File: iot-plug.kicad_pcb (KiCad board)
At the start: 2 copper layers, 55.4 x 52.2 mm, 32 parts, among them J1 Conn_01x02_Pin, J2 Conn_01x02_Pin, J3 USB_C_Receptacle_USB2.0_16P, K1 HF46F_005-HS1, Q2 2N3904, U1 ESP32-S3-MINI-1, U2 USBLC6-2SC6, U4 AMS1117-3.3

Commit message: from shivpc
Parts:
- added REF**: Symbol_HighVoltage_NoTriangle_2x5mm_Copper, Symbol:Symbol_HighVoltage_NoTriangle_2x5mm_Copper, F.Cu at (88.0, 100.5)

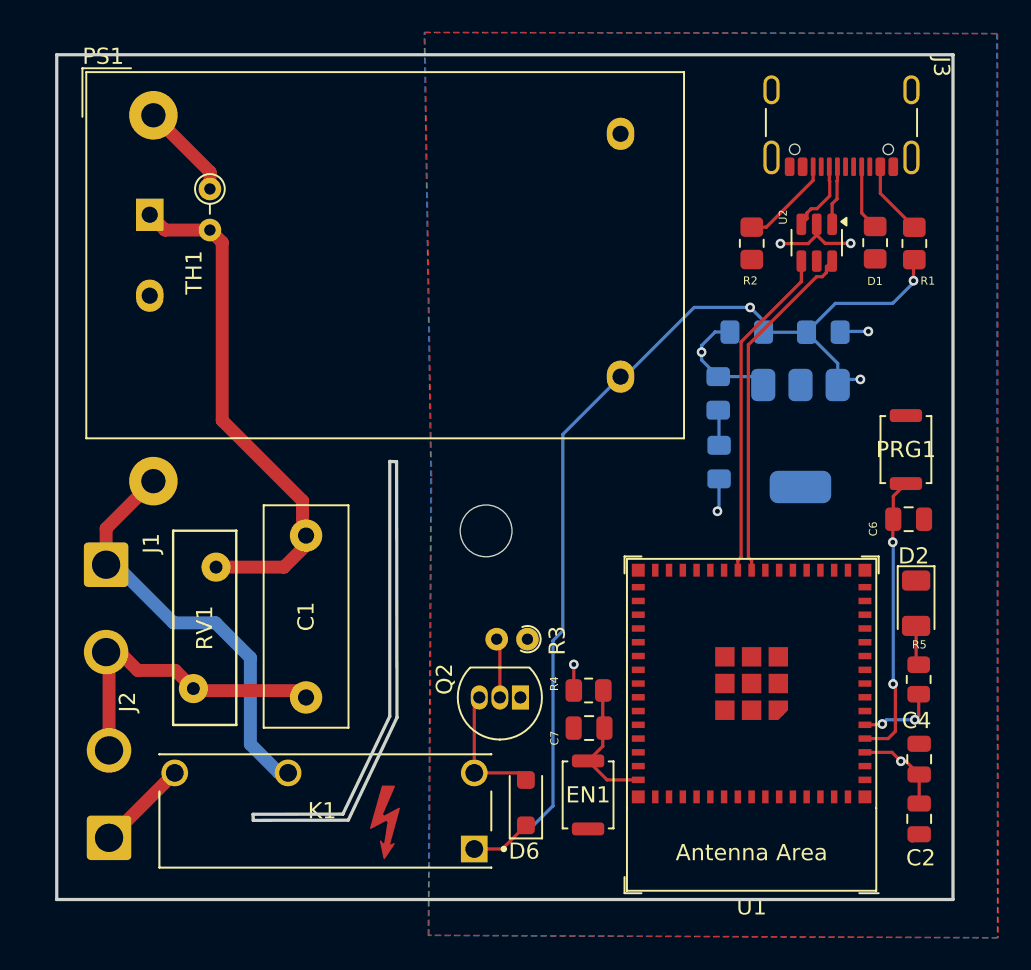
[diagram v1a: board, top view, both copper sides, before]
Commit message: layout updated
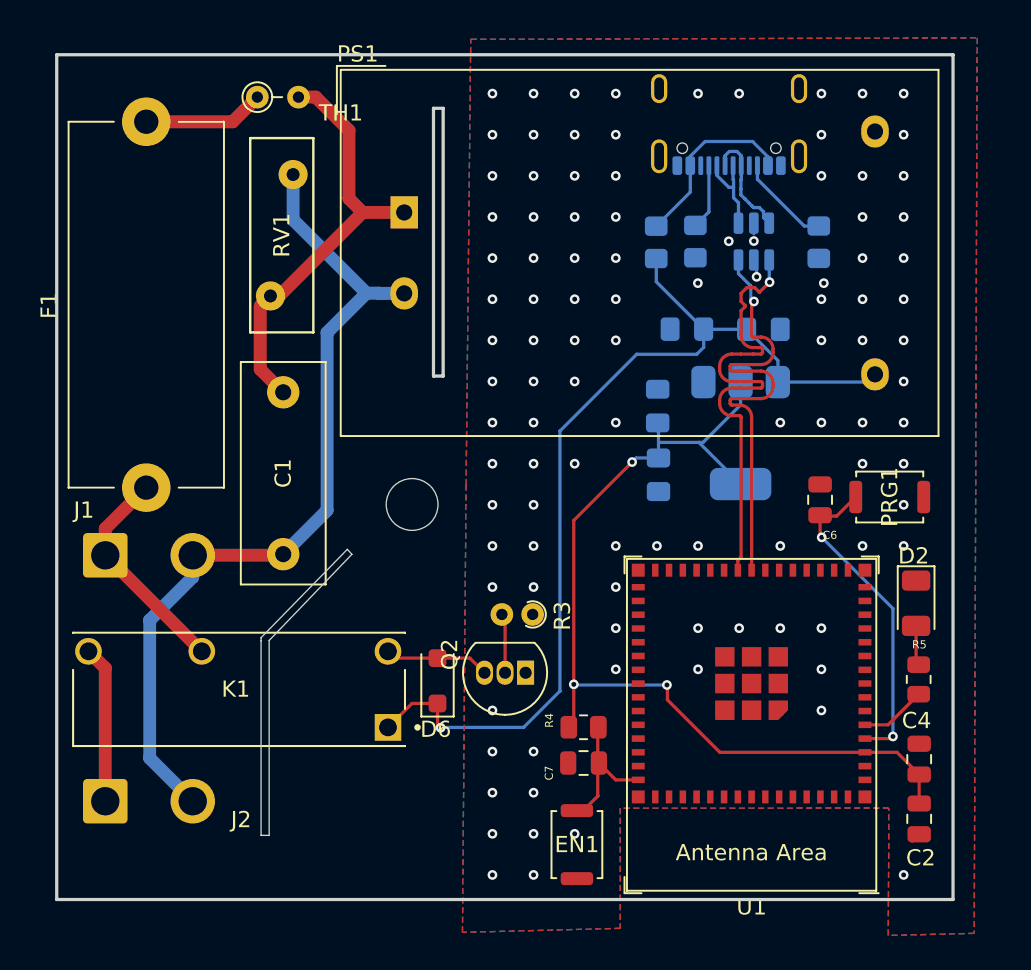
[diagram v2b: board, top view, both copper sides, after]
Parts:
- removed REF**: Symbol_HighVoltage_NoTriangle_2x5mm_Copper, Symbol:Symbol_HighVoltage_NoTriangle_2x5mm_Copper
- D1, J3, R1, R2, U2: moved to B.Cu
- F1: moved to F.Cu
- moved RV1 17.1 mm to (80.7, 67.8), turned to 90 degrees
- moved D1 15.9 mm to (104.5, 64.5)
- moved PS1 15.7 mm to (88.9, 62.7)
- moved R1 11.1 mm to (106.9, 64.5)
- moved D6 9.30 mm to (91.0, 91.6)
- moved K1 9.21 mm to (78.7, 92.1)
- moved C1 8.96 mm to (81.5, 73.8)
- moved J3 6.94 mm to (109.0, 56.1), turned to 0 degrees
- moved TH1 6.38 mm to (79.9, 55.6), turned to 0 degrees
- moved C6 5.60 mm to (114.6, 80.4), turned to 90 degrees
- moved H1 4.85 mm to (89.4, 80.7)
- moved R2 4.14 mm to (114.5, 64.5)
- moved U2 3.89 mm to (110.5, 64.5)
- moved C5 3.82 mm to (104.6, 74.6)
- moved CP2 3.82 mm to (104.7, 78.9)
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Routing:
- net 3V3: track 9.53 -> 58.9 mm, vias 2 -> 3
- net /N: track 19.7 -> 52.8 mm
- net GND: track 19.0 -> 3.33 mm, vias 5 -> 103
- net /P: track 26.1 -> 13.6 mm
- net /D+: track 25.2 -> 36.6 mm, vias 0 -> 1
- net /D-: track 25.2 -> 33.9 mm, vias 0 -> 1
- net Net-(D1-A): track 4.61 -> 11.3 mm
- net Net-(PS1-AC/L): track 32.7 -> 26.6 mm
- net L: track 5.72 -> 9.69 mm
- net 5V: track 63.5 -> 60.3 mm, vias 3 -> 1
- net /IO0: track 17.8 -> 20.5 mm
- net Net-(D6-A): track 8.16 -> 6.51 mm
- net Net-(F1-Pad2): track 6.00 -> 7.49 mm
- net /IO1: track 4.89 -> 4.10 mm, vias 2 -> 0
- added copper zone on B.Cu, net GND
- removed copper zone on B.Cu, net 3V3
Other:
- outline, holes or cut-outs redrawn

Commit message: logo added
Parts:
- added G***: LOGO, LOGO, F.Cu at (97.4, 81.4)
- added REF**: KiCad-Logo2_8mm_SilkScreen, Symbol:KiCad-Logo2_8mm_SilkScreen, F.Cu at (150.4, 87.0)
- added REF**: KiCad-Logo2_8mm_SilkScreen, Symbol:KiCad-Logo2_8mm_SilkScreen, F.Cu at (141.4, 86.5)
- moved H1 1.62 mm to (89.4, 82.3)
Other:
- board text added: "230V,10A"
- board text added: "AR RoboTics"
- board text added: "Home PlugX"
- board text added: "LOAD"
- board text added: "Made in India"

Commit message: updated tracks & nets
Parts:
- removed REF** (x2): KiCad-Logo2_8mm_SilkScreen, Symbol:KiCad-Logo2_8mm_SilkScreen
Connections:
- U1 pad 25: unconnected-(U1-GPIO21-Pad25) -> RL
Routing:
- net RL: track 0.00 -> 13.7 mm, vias 0 -> 1
- net 5V: track 60.3 -> 59.3 mm, vias 1 -> 5

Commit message: updated
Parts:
- moved J2 0.79 mm to (70.4, 99.8)
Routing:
- net /N: track 52.8 -> 53.5 mm
- net L: track 9.69 -> 10.4 mm
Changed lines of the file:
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@@
 	(footprint "Connector_Wire:SolderWire-1sqmm_1x02_P5.4mm_D1.4mm_OD2.7mm"
 		(layer "F.Cu")
-		(at 70.48 99.05)
+		(at 70.36 99.83)
 		(descr "Soldered wire connection, for 2 times 1 mm² wires, basic insulation, conductor diameter 1.4mm, outer diameter 2.7mm, size source Multi-Contact FLEXI-E 1.0 (https://ec.staubli.com/AcroFiles/Catalogues/TM_Cab-Main-11014119_(en)_hi.pdf), bend radius 3 times outer diameter, generated with kicad-footprint-generator")
 		(tags "connector wire 1sqmm")
@@
 	)
 	(gr_text "LOAD"
-		(at 71.12 103.45 0)
+		(at 71.03 103.95 0)
 		(layer "F.SilkS")
 		(effects
@@
 	)
 	(segment
-		(start 75.88 99.05)
-		(end 73.22 96.39)
+		(start 84.1765 81.0835)
+		(end 81.47 83.79)
 		(width 0.8)
 		(layer "B.Cu")
@@
 	)
 	(segment
-		(start 84.1765 81.0835)
-		(end 81.47 83.79)
+		(start 75.76 99.83)
+		(end 75.76 98.93)
 		(width 0.8)
 		(layer "B.Cu")
@@
 	)
 	(segment
-		(start 75.88 84.95)
-		(end 75.88 83.86)
+		(start 75.76 98.93)
+		(end 73.22 96.39)
 		(width 0.8)
 		(layer "B.Cu")
@@
 	)
 	(segment
-		(start 86.61 67.67)
-		(end 87.385 67.67)
+		(start 73.22 96.39)
+		(end 73.22 87.61)
 		(width 0.8)
 		(layer "B.Cu")
@@
 	)
 	(segment
-		(start 82.08 60.34)
-		(end 82.08 63.14)
+		(start 86.61 67.67)
+		(end 87.385 67.67)
 		(width 0.8)
 		(layer "B.Cu")
@@
 	)
 	(segment
-		(start 73.22 96.39)
-		(end 73.22 87.61)
+		(start 82.08 60.34)
+		(end 82.08 63.14)
+		(width 0.8)
+		(layer "B.Cu")
+		(net 51)
+	)
+	(segment
+		(start 75.88 84.95)
+		(end 75.88 83.86)
 		(width 0.8)
 		(layer "B.Cu")
@@
 	)
 	(segment
-		(start 69.87 98.44)
-		(end 69.87 90.22)
+		(start 70.36 99.83)
+		(end 70.36 98.93)
 		(width 0.8)
 		(layer "F.Cu")
@@
 	)
 	(segment
-		(start 70.48 99.05)
-		(end 69.87 98.44)
+		(start 69.87 90.22)
+		(end 69.44 89.79)
 		(width 0.8)
 		(layer "F.Cu")
@@
 	)
 	(segment
-		(start 69.87 90.22)
-		(end 69.44 89.79)
+		(start 69.87 98.44)
+		(end 69.87 90.22)
+		(width 0.8)
+		(layer "F.Cu")
+		(net 54)
+	)
+	(segment
+		(start 70.36 98.93)
+		(end 69.87 98.44)
 		(width 0.8)
 		(layer "F.Cu")
